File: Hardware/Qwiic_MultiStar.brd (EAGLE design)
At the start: 61.4 x 56.8 mm, 23 parts, among them J1 QWIIC_RIGHT_ANGLE, J2 QWIIC_RIGHT_ANGLE, J3 QWIIC_RIGHT_ANGLE, J4 QWIIC_RIGHT_ANGLE, J5 QWIIC_RIGHT_ANGLE

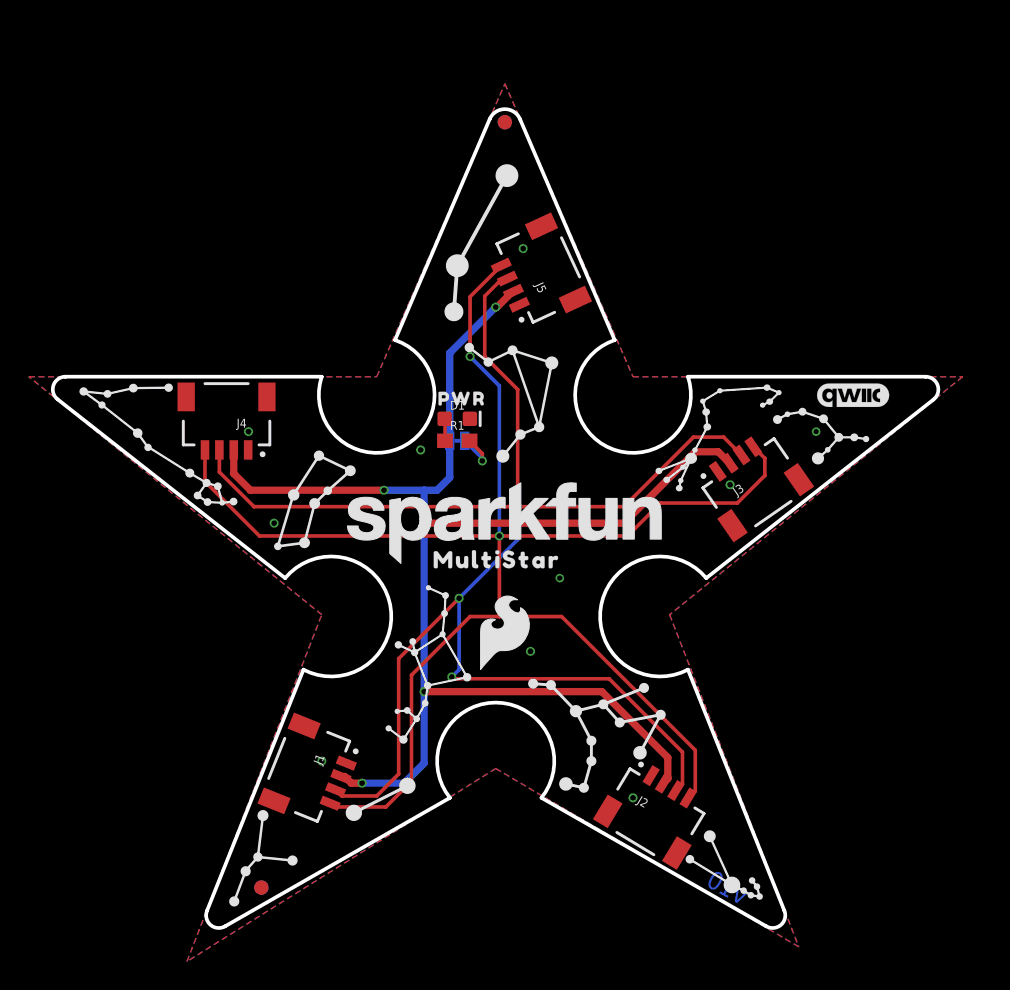
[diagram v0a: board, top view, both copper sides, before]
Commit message: Made the dimensions symmetrical
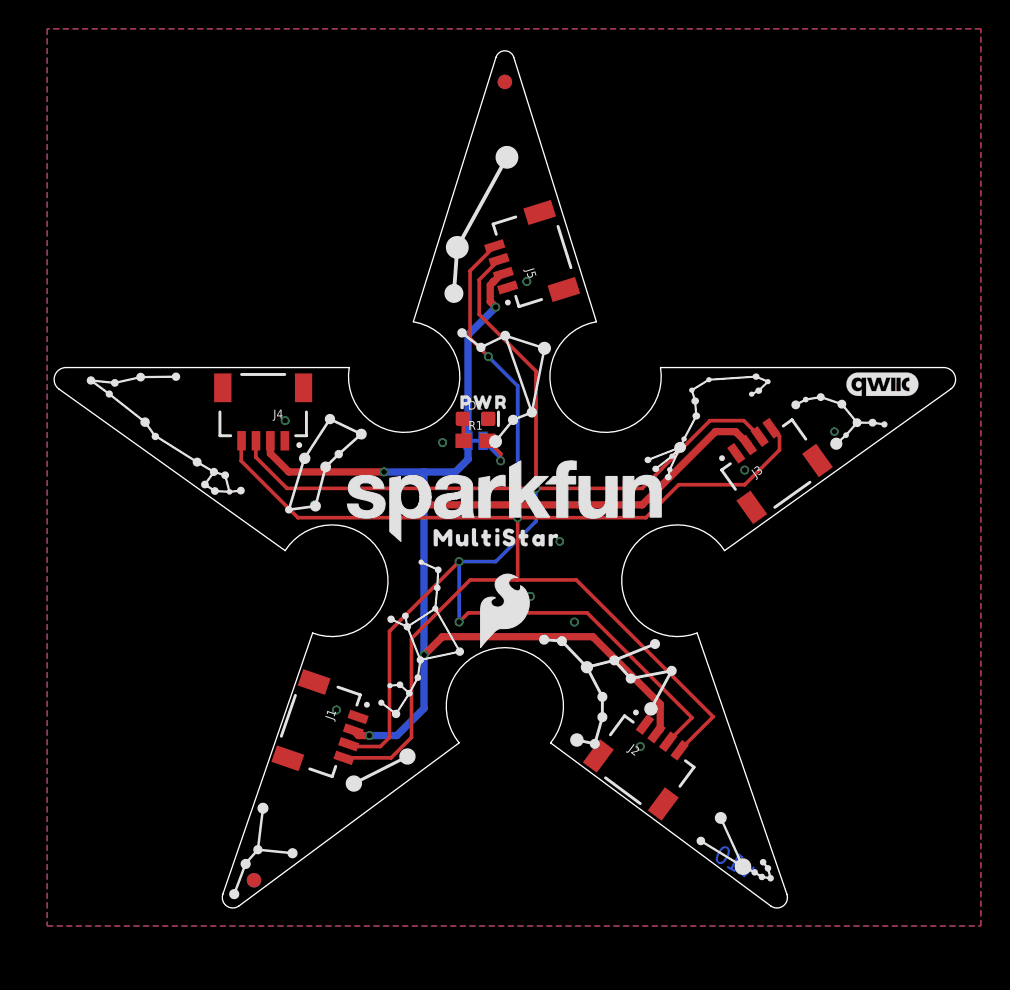
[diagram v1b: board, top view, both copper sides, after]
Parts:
- moved FRAME1 8.03 mm to (14.0, -11.4)
- moved J2 3.47 mm to (42.7, 13.1), turned to 323.5 degrees
- moved J1 3.30 mm to (21.1, 13.1), turned to 251 degrees
- moved FD3 2.79 mm to (31.8, 58.5)
- moved FD4 2.79 mm to (31.8, 58.5)
- moved J4 2.62 mm to (15.0, 33.7)
- moved LOGO1 2.17 mm to (57.9, 37.6)
- moved LOGO2 2.17 mm to (57.9, 37.6)
- moved LOGO3 1.85 mm to (31.6, 22.1)
- moved J3 1.80 mm to (49.0, 33.7), turned to 35.5 degrees
- moved U$9 1.55 mm to (27.9, 36.3)
- moved U$2 1.52 mm to (31.8, 21.8)
- moved U$3 1.52 mm to (25.9, 26.9)
- moved U$5 1.52 mm to (36.3, 26.9)
- moved LOGO4 1.52 mm to (31.8, 29.5)
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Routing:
- net SCL: track 115.3 -> 111.2 mm
- net 3.3V: track 102.0 -> 97.9 mm
- net SDA: track 112.7 -> 109.5 mm
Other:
- board size 61.4 x 56.8 mm -> 62.5 x 59.5 mm
